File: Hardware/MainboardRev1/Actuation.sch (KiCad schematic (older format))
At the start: 28 parts, among them J3 Servo_Control, J4 CONN_01X02, J5 CONN_01X02, Q14 SSM3J328R, Q15 NTR4003, Q16 SSM3J328R, Q17 SSM3J328R, Q18 NTR4003, Q19 NTR4003, Q20 SIS612EDNT-T1-GE3, Q21 SIS612EDNT-T1-GE3, U10 LTC4358

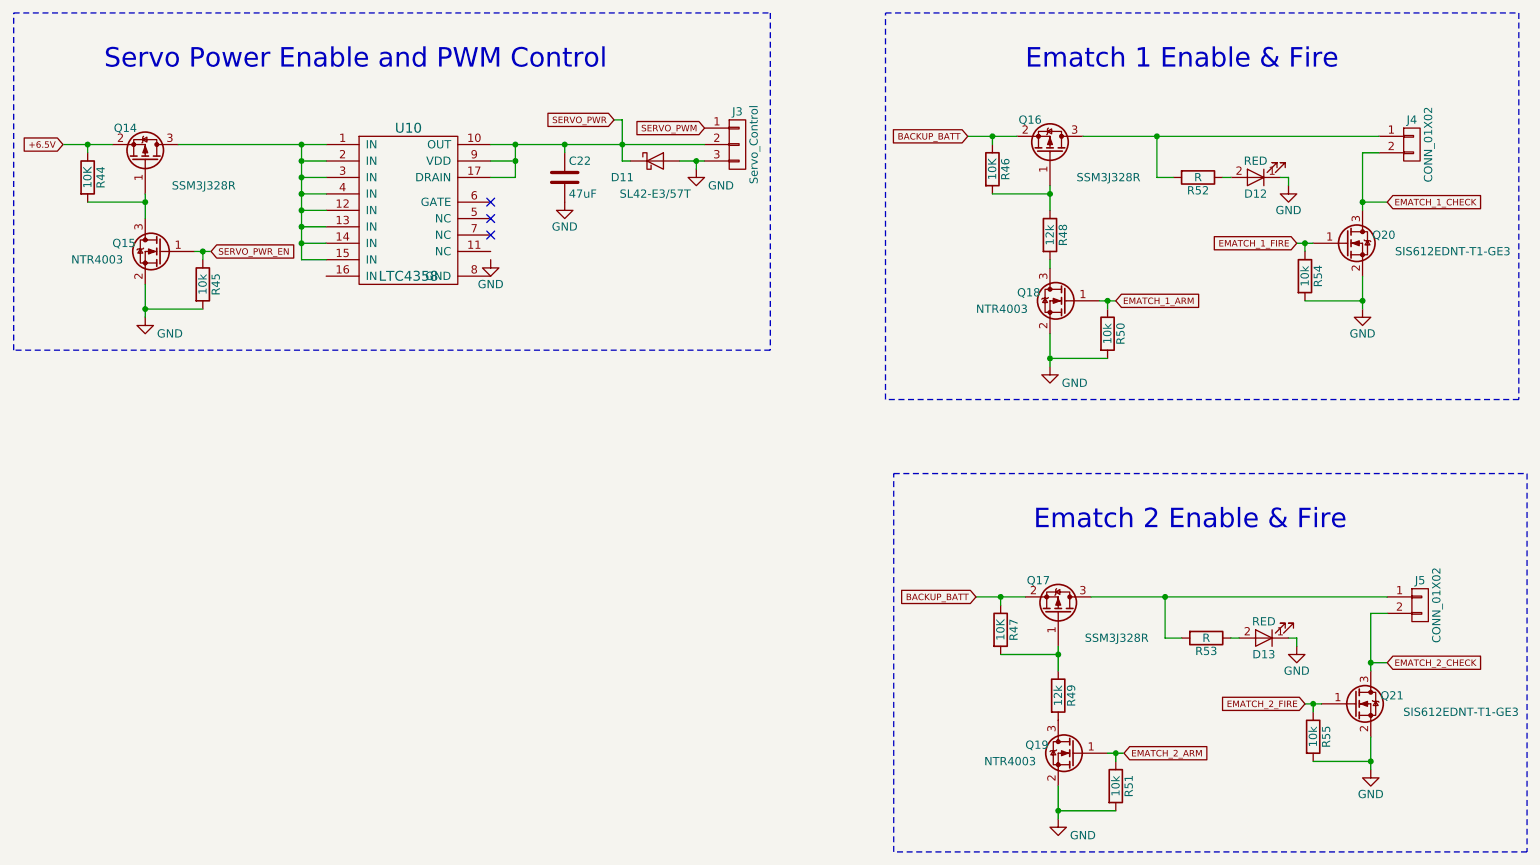
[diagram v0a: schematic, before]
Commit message: Small changes to schematic: Added voltage dividers for analog inputs, small net changes. Added footprints for each part
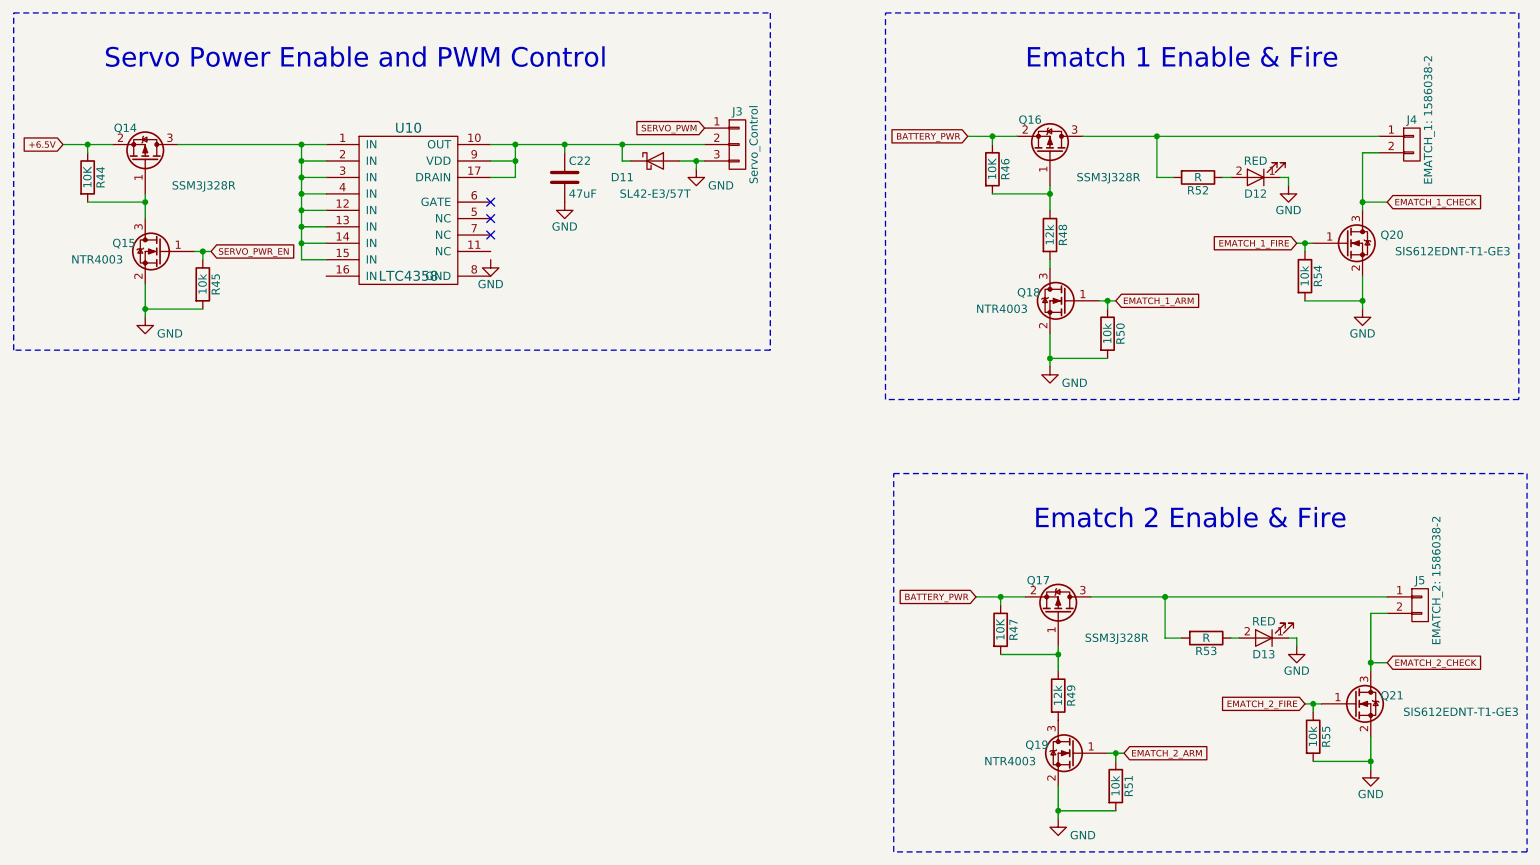
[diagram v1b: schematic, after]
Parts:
- C22: footprint (none) -> Capacitors_SMD:C_1210_HandSoldering
- D11: footprint (none) -> Dans_Parts:DO-214AB_Zener
- D12, D13: footprint (none) -> LEDs:LED_0603_HandSoldering
- J3: footprint (none) -> Dans_Parts:Molex_Microfit3_Header_01x03_Straight
- J4: value CONN_01X02 -> EMATCH_1: 1586038-2; footprint (none) -> Dans_Parts:CONN_2POS_VERT_TE_CONN
- J5: value CONN_01X02 -> EMATCH_2: 1586038-2; footprint (none) -> Dans_Parts:CONN_2POS_VERT_TE_CONN
- Q14, Q15, Q16, Q17, Q18, Q19: footprint (none) -> TO_SOT_Packages_SMD:SOT-23
- Q20, Q21: footprint (none) -> Dans_Parts:PowerPAK_1212-8S
- R44, R45, R46, R47, R48, R49, R50, R51, R52, R53, R54, R55: footprint (none) -> Resistors_SMD:R_0603_HandSoldering
- U10: footprint (none) -> Housings_SSOP:TSSOP-14-1EP_4.4x5mm_Pitch0.65mm
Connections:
- net BACKUP_BATT renamed BATTERY_PWR
- net SERVO_PWR: no longer names the net of C22.1, D11.1 (K), J3.2 (P2), U10.10 (OUT), U10.17 (DRAIN), U10.9 (VDD)
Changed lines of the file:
@@
 F 0 "U10" H 3400 2650 60  0000 C CNN
 F 1 "LTC4358" H 3400 1750 60  0000 C CNN
-F 2 "" H 3400 1900 60  0001 C CNN
+F 2 "Housings_SSOP:TSSOP-14-1EP_4.4x5mm_Pitch0.65mm" H 3400 1900 60  0001 C CNN
 F 3 "" H 3400 1900 60  0001 C CNN
 	1    3400 2200
@@
 F 0 "Q14" V 2000 1900 50  0000 R CNN
 F 1 "SSM3J328R" V 1650 2500 50  0000 R CNN
-F 2 "" H 2000 2050 50  0000 C CNN
+F 2 "TO_SOT_Packages_SMD:SOT-23" H 2000 2050 50  0001 C CNN
 F 3 "" H 1800 1950 50  0000 C CNN
 	1    1800 1950
@@
 F 0 "R44" V 1530 2050 50  0000 C CNN
 F 1 "10K" V 1450 2050 50  0000 C CNN
-F 2 "" V 1380 2050 50  0000 C CNN
+F 2 "Resistors_SMD:R_0603_HandSoldering" V 1380 2050 50  0001 C CNN
 F 3 "" H 1450 2050 50  0000 C CNN
 	1    1450 2050
@@
 F 0 "R45" V 2230 2700 50  0000 C CNN
 F 1 "10k" V 2150 2700 50  0000 C CNN
-F 2 "" V 2080 2700 50  0000 C CNN
+F 2 "Resistors_SMD:R_0603_HandSoldering" V 2080 2700 50  0001 C CNN
 F 3 "" H 2150 2700 50  0000 C CNN
 	1    2150 2700
@@
 F 0 "Q15" H 2200 2550 50  0000 R CNN
 F 1 "NTR4003" H 2450 2450 50  0000 R CNN
-F 2 "" H 2100 2600 50  0000 C CNN
+F 2 "TO_SOT_Packages_SMD:SOT-23" H 2100 2600 50  0001 C CNN
 F 3 "" H 1900 2500 50  0000 C CNN
 	1    1900 2500
@@
 F 0 "C22" H 4375 2150 50  0000 L CNN
 F 1 "47uF" H 4375 1950 50  0000 L CNN
-F 2 "" H 4388 1900 50  0000 C CNN
+F 2 "Capacitors_SMD:C_1210_HandSoldering" H 4388 1900 50  0001 C CNN
 F 3 "" H 4350 2050 50  0000 C CNN
 	1    4350 2050
@@
 	1    0    0    -1
 $EndComp
-Text GLabel 4650 1700 0    39   Input ~ 0
-SERVO_PWR
 $Comp
 L GND #PWR039
@@
 F 0 "J3" H 5400 2050 50  0000 C CNN
 F 1 "Servo_Control" V 5500 1850 50  0000 C CNN
-F 2 "" H 5400 1850 50  0000 C CNN
+F 2 "Dans_Parts:Molex_Microfit3_Header_01x03_Straight" H 5400 1850 50  0001 C CNN
 F 3 "" H 5400 1850 50  0000 C CNN
 	1    5400 1850
@@
 Wire Wire Line
 	4700 1950 4750 1950
-Wire Wire Line
-	4650 1700 4700 1700
-Wire Wire Line
-	4700 1700 4700 1950
 Text GLabel 5200 1750 0    39   Input ~ 0
 SERVO_PWM
@@
 F 0 "D11" H 4700 1850 50  0000 C CNN
 F 1 "SL42-E3/57T" H 4900 1750 50  0000 C CNN
-F 2 "" H 4900 1950 50  0000 C CNN
+F 2 "Dans_Parts:DO-214AB_Zener" H 4900 1950 50  0001 C CNN
 F 3 "" H 4900 1950 50  0000 C CNN
 	1    4900 1950
@@
 F 0 "Q16" V 7500 1850 50  0000 R CNN
 F 1 "SSM3J328R" V 7150 2450 50  0000 R CNN
-F 2 "" H 7500 2000 50  0000 C CNN
+F 2 "TO_SOT_Packages_SMD:SOT-23" H 7500 2000 50  0001 C CNN
 F 3 "" H 7300 1900 50  0000 C CNN
 	1    7300 1900
@@
 F 0 "R46" V 7030 2000 50  0000 C CNN
 F 1 "10K" V 6950 2000 50  0000 C CNN
-F 2 "" V 6880 2000 50  0000 C CNN
+F 2 "Resistors_SMD:R_0603_HandSoldering" V 6880 2000 50  0001 C CNN
 F 3 "" H 6950 2000 50  0000 C CNN
 	1    6950 2000
@@
 F 0 "R50" V 7730 3000 50  0000 C CNN
 F 1 "10k" V 7650 3000 50  0000 C CNN
-F 2 "" V 7580 3000 50  0000 C CNN
+F 2 "Resistors_SMD:R_0603_HandSoldering" V 7580 3000 50  0001 C CNN
 F 3 "" H 7650 3000 50  0000 C CNN
 	1    7650 3000
@@
 F 0 "Q18" H 7700 2850 50  0000 R CNN
 F 1 "NTR4003" H 7950 2750 50  0000 R CNN
-F 2 "" H 7600 2900 50  0000 C CNN
+F 2 "TO_SOT_Packages_SMD:SOT-23" H 7600 2900 50  0001 C CNN
 F 3 "" H 7400 2800 50  0000 C CNN
 	1    7400 2800
@@
 	6800 1800 7100 1800
 Text GLabel 6800 1800 0    39   Input ~ 0
-BACKUP_BATT
+BATTERY_PWR
 $Comp
 L CONN_01X02 J4
@@
 P 9500 1850
 F 0 "J4" H 9500 2000 50  0000 C CNN
-F 1 "CONN_01X02" V 9600 1850 50  0000 C CNN
-F 2 "" H 9500 1850 50  0000 C CNN
+F 1 "EMATCH_1: 1586038-2" V 9600 2000 50  0000 C CNN
+F 2 "Dans_Parts:CONN_2POS_VERT_TE_CONN" H 9500 1850 50  0001 C CNN
 F 3 "" H 9500 1850 50  0000 C CNN
 	1    9500 1850
@@
 U 1 1 5AFA7B1B
 P 9100 2450
-F 0 "Q20" H 9400 2500 50  0000 R CNN
+F 0 "Q20" H 9450 2500 50  0000 R CNN
 F 1 "SIS612EDNT-T1-GE3" H 10100 2400 50  0000 R CNN
-F 2 "" H 9300 2550 50  0000 C CNN
+F 2 "Dans_Parts:PowerPAK_1212-8S" H 9300 2550 50  0001 C CNN
 F 3 "" H 9100 2450 50  0000 C CNN
 	1    9100 2450
@@
 F 0 "R54" V 8930 2650 50  0000 C CNN
 F 1 "10k" V 8850 2650 50  0000 C CNN
-F 2 "" V 8780 2650 50  0000 C CNN
+F 2 "Resistors_SMD:R_0603_HandSoldering" V 8780 2650 50  0001 C CNN
 F 3 "" H 8850 2650 50  0000 C CNN
 	1    8850 2650
@@
 F 0 "D12" H 8550 2150 50  0000 C CNN
 F 1 "RED" H 8550 1950 50  0000 C CNN
-F 2 "" H 8550 2050 50  0000 C CNN
+F 2 "LEDs:LED_0603_HandSoldering" H 8550 2050 50  0001 C CNN
 F 3 "" H 8550 2050 50  0000 C CNN
 	1    8550 2050
@@
 F 0 "R52" V 8280 2050 50  0000 C CNN
 F 1 "R" V 8200 2050 50  0000 C CNN
-F 2 "" V 8130 2050 50  0000 C CNN
+F 2 "Resistors_SMD:R_0603_HandSoldering" V 8130 2050 50  0001 C CNN
 F 3 "" H 8200 2050 50  0000 C CNN
 	1    8200 2050
@@
 F 0 "Q17" V 7550 4650 50  0000 R CNN
 F 1 "SSM3J328R" V 7200 5250 50  0000 R CNN
-F 2 "" H 7550 4800 50  0000 C CNN
+F 2 "TO_SOT_Packages_SMD:SOT-23" H 7550 4800 50  0001 C CNN
 F 3 "" H 7350 4700 50  0000 C CNN
 	1    7350 4700
@@
 F 0 "R47" V 7080 4800 50  0000 C CNN
 F 1 "10K" V 7000 4800 50  0000 C CNN
-F 2 "" V 6930 4800 50  0000 C CNN
+F 2 "Resistors_SMD:R_0603_HandSoldering" V 6930 4800 50  0001 C CNN
 F 3 "" H 7000 4800 50  0000 C CNN
 	1    7000 4800
@@
 F 0 "R51" V 7780 5750 50  0000 C CNN
 F 1 "10k" V 7700 5750 50  0000 C CNN
-F 2 "" V 7630 5750 50  0000 C CNN
+F 2 "Resistors_SMD:R_0603_HandSoldering" V 7630 5750 50  0001 C CNN
 F 3 "" H 7700 5750 50  0000 C CNN
 	1    7700 5750
@@
 F 0 "Q19" H 7750 5600 50  0000 R CNN
 F 1 "NTR4003" H 8000 5500 50  0000 R CNN
-F 2 "" H 7650 5650 50  0000 C CNN
+F 2 "TO_SOT_Packages_SMD:SOT-23" H 7650 5650 50  0001 C CNN
 F 3 "" H 7450 5550 50  0000 C CNN
 	1    7450 5550
@@
 	6850 4600 7150 4600
 Text GLabel 6850 4600 0    39   Input ~ 0
-BACKUP_BATT
+BATTERY_PWR
 $Comp
 L CONN_01X02 J5
@@
 P 9550 4650
 F 0 "J5" H 9550 4800 50  0000 C CNN
-F 1 "CONN_01X02" V 9650 4650 50  0000 C CNN
-F 2 "" H 9550 4650 50  0000 C CNN
+F 1 "EMATCH_2: 1586038-2" V 9650 4800 50  0000 C CNN
+F 2 "Dans_Parts:CONN_2POS_VERT_TE_CONN" H 9550 4650 50  0001 C CNN
 F 3 "" H 9550 4650 50  0000 C CNN
 	1    9550 4650
@@
 F 0 "Q21" H 9450 5300 50  0000 R CNN
 F 1 "SIS612EDNT-T1-GE3" H 10150 5200 50  0000 R CNN
-F 2 "" H 9350 5350 50  0000 C CNN
+F 2 "Dans_Parts:PowerPAK_1212-8S" H 9350 5350 50  0001 C CNN
 F 3 "" H 9150 5250 50  0000 C CNN
 	1    9150 5250
@@
 F 0 "R55" V 8980 5450 50  0000 C CNN
 F 1 "10k" V 8900 5450 50  0000 C CNN
-F 2 "" V 8830 5450 50  0000 C CNN
+F 2 "Resistors_SMD:R_0603_HandSoldering" V 8830 5450 50  0001 C CNN
 F 3 "" H 8900 5450 50  0000 C CNN
 	1    8900 5450
@@
 F 0 "D13" H 8600 4950 50  0000 C CNN
 F 1 "RED" H 8600 4750 50  0000 C CNN
-F 2 "" H 8600 4850 50  0000 C CNN
+F 2 "LEDs:LED_0603_HandSoldering" H 8600 4850 50  0001 C CNN
 F 3 "" H 8600 4850 50  0000 C CNN
 	1    8600 4850
@@
 F 0 "R53" V 8330 4850 50  0000 C CNN
 F 1 "R" V 8250 4850 50  0000 C CNN
-F 2 "" V 8180 4850 50  0000 C CNN
+F 2 "Resistors_SMD:R_0603_HandSoldering" V 8180 4850 50  0001 C CNN
 F 3 "" H 8250 4850 50  0000 C CNN
 	1    8250 4850
@@
 F 0 "R48" V 7380 2400 50  0000 C CNN
 F 1 "12k" V 7300 2400 50  0000 C CNN
-F 2 "" V 7230 2400 50  0001 C CNN
+F 2 "Resistors_SMD:R_0603_HandSoldering" V 7230 2400 50  0001 C CNN
 F 3 "" H 7300 2400 50  0001 C CNN
 	1    7300 2400
@@
 F 0 "R49" V 7430 5200 50  0000 C CNN
 F 1 "12k" V 7350 5200 50  0000 C CNN
-F 2 "" V 7280 5200 50  0001 C CNN
+F 2 "Resistors_SMD:R_0603_HandSoldering" V 7280 5200 50  0001 C CNN
 F 3 "" H 7350 5200 50  0001 C CNN
 	1    7350 5200
 	1    0    0    -1
 $EndComp
+Wire Wire Line
+	4700 1950 4700 1850
 $EndSCHEMATC

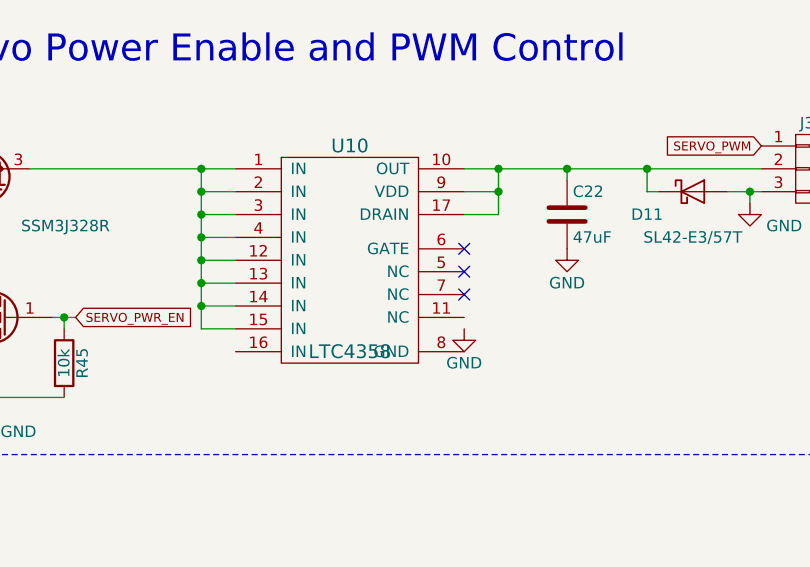
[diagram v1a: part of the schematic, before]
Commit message: Components placed. Needs to be routed.
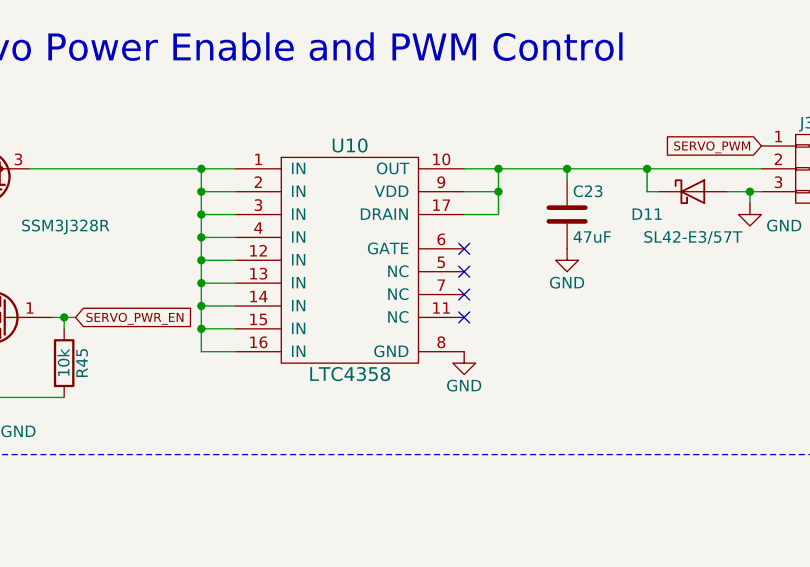
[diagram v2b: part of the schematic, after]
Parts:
- U10: footprint Housings_SSOP:TSSOP-14-1EP_4.4x5mm_Pitch0.65mm -> Housings_SSOP:HTSSOP-16-1EP_4.4x5mm_Pitch0.65mm
- renumbered C22 to C23
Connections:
- net GND: now also U10.8 (GND)
- net at Q14.3 (D), U10.1 (IN), U10.12 (IN)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: now also U10.16 (IN)
- no-connect marks 3 -> 4
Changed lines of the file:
@@
 LIBS:teensy3_6-OuterHeadersOnly
 LIBS:switches
+LIBS:mounting_hole_eighth_inch
 LIBS:MainboardRev1-cache
 EELAYER 25 0
@@
 P 3400 2200
 F 0 "U10" H 3400 2650 60  0000 C CNN
-F 1 "LTC4358" H 3400 1750 60  0000 C CNN
-F 2 "Housings_SSOP:TSSOP-14-1EP_4.4x5mm_Pitch0.65mm" H 3400 1900 60  0001 C CNN
+F 1 "LTC4358" H 3400 1650 60  0000 C CNN
+F 2 "Housings_SSOP:HTSSOP-16-1EP_4.4x5mm_Pitch0.65mm" H 3400 1900 60  0001 C CNN
 F 3 "" H 3400 1900 60  0001 C CNN
 	1    3400 2200
@@
 +6.5V
 $Comp
-L GND #PWR036
+L GND #PWR042
 U 1 1 5AF9BFAC
-P 3900 2550
-F 0 "#PWR036" H 3900 2300 50  0001 C CNN
-F 1 "GND" H 3900 2400 50  0000 C CNN
-F 2 "" H 3900 2550 50  0000 C CNN
-F 3 "" H 3900 2550 50  0000 C CNN
-	1    3900 2550
+P 3900 2650
+F 0 "#PWR042" H 3900 2400 50  0001 C CNN
+F 1 "GND" H 3900 2500 50  0000 C CNN
+F 2 "" H 3900 2650 50  0000 C CNN
+F 3 "" H 3900 2650 50  0000 C CNN
+	1    3900 2650
 	1    0    0    -1
 $EndComp
@@
 $EndComp
 $Comp
-L GND #PWR037
+L GND #PWR043
 U 1 1 5AF9DC38
 P 1800 2900
-F 0 "#PWR037" H 1800 2650 50  0001 C CNN
+F 0 "#PWR043" H 1800 2650 50  0001 C CNN
 F 1 "GND" H 1950 2800 50  0000 C CNN
 F 2 "" H 1800 2900 50  0000 C CNN
@@
 SERVO_PWR_EN
 $Comp
-L C C22
+L C C23
 U 1 1 5AF9DFB4
 P 4350 2050
-F 0 "C22" H 4375 2150 50  0000 L CNN
+F 0 "C23" H 4375 2150 50  0000 L CNN
 F 1 "47uF" H 4375 1950 50  0000 L CNN
 F 2 "Capacitors_SMD:C_1210_HandSoldering" H 4388 1900 50  0001 C CNN
@@
 $EndComp
 $Comp
-L GND #PWR038
+L GND #PWR044
 U 1 1 5AF9E058
 P 4350 2200
-F 0 "#PWR038" H 4350 1950 50  0001 C CNN
+F 0 "#PWR044" H 4350 1950 50  0001 C CNN
 F 1 "GND" H 4350 2050 50  0000 C CNN
 F 2 "" H 4350 2200 50  0000 C CNN
@@
 $EndComp
 $Comp
-L GND #PWR039
+L GND #PWR045
 U 1 1 5AF9E824
 P 5150 2000
-F 0 "#PWR039" H 5150 1750 50  0001 C CNN
+F 0 "#PWR045" H 5150 1750 50  0001 C CNN
 F 1 "GND" H 5300 1900 50  0000 C CNN
 F 2 "" H 5150 2000 50  0000 C CNN
@@
 	2750 2550 2900 2550
 Wire Wire Line
-	2750 1850 2750 2550
+	2750 1850 2750 2650
 Wire Wire Line
 	2750 2450 2900 2450
@@
 $EndComp
 $Comp
-L GND #PWR040
+L GND #PWR046
 U 1 1 5AFA686D
 P 7300 3200
-F 0 "#PWR040" H 7300 2950 50  0001 C CNN
+F 0 "#PWR046" H 7300 2950 50  0001 C CNN
 F 1 "GND" H 7450 3100 50  0000 C CNN
 F 2 "" H 7300 3200 50  0000 C CNN
@@
 	9200 2650 9200 2850
 $Comp
-L GND #PWR041
+L GND #PWR047
 U 1 1 5AFA7F4E
 P 9200 2850
-F 0 "#PWR041" H 9200 2600 50  0001 C CNN
+F 0 "#PWR047" H 9200 2600 50  0001 C CNN
 F 1 "GND" H 9200 2700 50  0000 C CNN
 F 2 "" H 9200 2850 50  0000 C CNN
@@
 $EndComp
 $Comp
-L GND #PWR042
+L GND #PWR048
 U 1 1 5AFAA805
 P 8750 2100
-F 0 "#PWR042" H 8750 1850 50  0001 C CNN
+F 0 "#PWR048" H 8750 1850 50  0001 C CNN
 F 1 "GND" H 8750 1950 50  0000 C CNN
 F 2 "" H 8750 2100 50  0000 C CNN
@@
 $EndComp
 $Comp
-L GND #PWR043
+L GND #PWR049
 U 1 1 5AFAB322
 P 7350 5950
-F 0 "#PWR043" H 7350 5700 50  0001 C CNN
+F 0 "#PWR049" H 7350 5700 50  0001 C CNN
 F 1 "GND" H 7500 5850 50  0000 C CNN
 F 2 "" H 7350 5950 50  0000 C CNN
@@
 	9250 5450 9250 5650
 $Comp
-L GND #PWR044
+L GND #PWR050
 U 1 1 5AFAB35E
 P 9250 5650
-F 0 "#PWR044" H 9250 5400 50  0001 C CNN
+F 0 "#PWR050" H 9250 5400 50  0001 C CNN
 F 1 "GND" H 9250 5500 50  0000 C CNN
 F 2 "" H 9250 5650 50  0000 C CNN
@@
 $EndComp
 $Comp
-L GND #PWR045
+L GND #PWR051
 U 1 1 5AFAB370
 P 8800 4900
-F 0 "#PWR045" H 8800 4650 50  0001 C CNN
+F 0 "#PWR051" H 8800 4650 50  0001 C CNN
 F 1 "GND" H 8800 4750 50  0000 C CNN
 F 2 "" H 8800 4900 50  0000 C CNN
@@
 Wire Wire Line
 	4700 1950 4700 1850
+Wire Wire Line
+	2750 2650 2900 2650
+Connection ~ 2750 2550
+NoConn ~ 3900 2500
 $EndSCHEMATC
